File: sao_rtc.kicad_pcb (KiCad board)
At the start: 2 copper layers, 44.9 x 32.9 mm, 40 parts, among them J1 S2B-PH-K-S(LF)(SN), J2 Conn_02x03_Odd_Even, J3 Conn_02x03_Odd_Even, P1 USB_C_Plug_USB2.0, SW1 DPDT, U1 AW32001ECSR, U2 PCF8563DRG, U3 M3410, Y1 32.768 kHz

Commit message: Complete 1st Draft
First Draft at Schematic Capture and Layout
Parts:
- removed C3: 1μF, sao:C_0603_1608Metric
- removed C4, C8: 4.7μF, sao:C_0603_1608Metric
- removed C5: C, Capacitor_THT:C_Disc_D3.0mm_W1.6mm_P2.50mm
- removed CLK0, VMON1: TestPoint, TestPoint:TestPoint_Loop_D2.50mm_Drill1.0mm
- removed D2: 4.3V, Diode_SMD:D_SOD-323_HandSoldering
- removed R2, R5: Ω, Resistor_SMD:R_0603_1608Metric
- removed R4: 10kΩ, Resistor_SMD:R_0603_1608Metric
- removed SW1: DPDT, Button_Switch_SMD:SW_DPDT_CK_JS202011JCQN
- removed TH1: Thermistor_NTC, Resistor_SMD:R_0603_1608Metric
- added C12: 47nF, Capacitor_SMD:C_0603_1608Metric, F.Cu at (97.6, 71.4)
- added C13: 10uF, Capacitor_SMD:C_0603_1608Metric, F.Cu at (91.3, 74.0)
- added C14: 10uF, Capacitor_SMD:C_0603_1608Metric, F.Cu at (94.6, 76.9)
- added C15: 10uF, Capacitor_SMD:C_0603_1608Metric, F.Cu at (91.3, 75.6)
- added C16: 22uF, Capacitor_SMD:C_0603_1608Metric, F.Cu at (109.8, 79.0)
- added C17: 22uF, Capacitor_SMD:C_0603_1608Metric, F.Cu at (94.9, 80.7)
- added C18: 47nF, Capacitor_SMD:C_0603_1608Metric, F.Cu at (108.3, 88.4)
- added C19: 47nF, Capacitor_SMD:C_0603_1608Metric, F.Cu at (110.5, 88.4)
- added D6: D, Diode_SMD:D_SMA, F.Cu at (107.0, 60.0)
- added D7: STAT, LED_SMD:LED_0603_1608Metric, F.Cu at (82.4, 84.1)
- added FB1: FerriteBead, Inductor_SMD:L_TDK_NLV32_3.2x2.5mm, F.Cu at (109.0, 81.4)
- added JP1: PH2.54-1x3P, Connector_PinHeader_2.54mm:PinHeader_1x03_P2.54mm_Vertical, F.Cu at (82.5, 68.0)
- added L3: 1uH, Inductor_SMD:L_1008_2520Metric, F.Cu at (94.9, 74.6)
- added R10: 10kΩ, Resistor_SMD:R_0603_1608Metric, F.Cu at (85.5, 68.3)
- added R12: 5.36k, Resistor_SMD:R_0603_1608Metric, F.Cu at (86.0, 71.5)
- added R13: 31.6k, Resistor_SMD:R_0603_1608Metric, F.Cu at (86.0, 73.4)
- added R15: 22Ω, Resistor_SMD:R_0603_1608Metric, F.Cu at (82.4, 82.5)
- added R16: 10kΩ, Resistor_SMD:R_0603_1608Metric, F.Cu at (82.4, 89.1)
- added R17: 10kΩ, Resistor_SMD:R_0603_1608Metric, F.Cu at (82.4, 80.8)
- added R18: 232, Resistor_SMD:R_0603_1608Metric, F.Cu at (89.9, 71.6)
- added TP1: TestPoint, TestPoint:TestPoint_Loop_D2.60mm_Drill1.4mm_Beaded, F.Cu at (114.5, 80.0)
- added TP2: TestPoint, TestPoint:TestPoint_Loop_D2.60mm_Drill1.4mm_Beaded, F.Cu at (114.5, 75.0)
- added TP3: TP_BATT, TestPoint:TestPoint_Loop_D2.60mm_Drill1.4mm_Beaded, F.Cu at (82.5, 58.9)
- added TP4: TP_PGOOD, TestPoint:TestPoint_Loop_D2.60mm_Drill1.4mm_Beaded, F.Cu at (82.5, 63.5)
- added TP5: TP_BMS, TestPoint:TestPoint_Loop_D2.60mm_Drill1.4mm_Beaded, F.Cu at (82.7, 77.5)
- added TP6: TP_VMON, TestPoint:TestPoint_Loop_D2.60mm_Drill1.4mm_Beaded, F.Cu at (114.5, 70.0)
- added TP7: TP_3V3, TestPoint:TestPoint_Loop_D2.60mm_Drill1.4mm_Beaded, F.Cu at (114.5, 85.0)
- added U5: XB7608AJ, sao:CPC-5_2.6mmx4mm_P0.53mm, F.Cu at (87.1, 59.9)
- C1: value 2.2μF -> 22uF
- C11: value 12uF -> 1μF
- C2: footprint sao:C_0603_1608Metric -> Capacitor_SMD:C_0603_1608Metric
- C7: value ~ -> 10μF
- D5: value RTC ON -> PGOOD
- J2: value Conn_02x03_Odd_Even -> Connector, In
- J3: value Conn_02x03_Odd_Even -> Connector, Out; footprint Swadge_Parts:PinSocket_2x03_P2.54mm_Vertical -> sao:PinHeader_2x03_P2.54mm_Vertical_Flipped
- L2: footprint Inductor_SMD:L_0603_1608Metric -> Inductor_SMD:L_1008_2520Metric
- U1: value AW32001ECSR -> BQ24259; footprint Package_CSP:WLCSP-9_1.21x1.22mm_Layout3x3_P0.4mm -> Package_DFN_QFN:HVQFN-24-1EP_4x4mm_P0.5mm_EP2.6x2.6mm_ThermalVias
- U3: value M3410 -> MT3410
- moved R14 43.2 mm to (82.4, 87.4)
- moved D5 43.1 mm to (82.4, 85.8)
- moved R11 39.2 mm to (82.4, 90.8), turned to 0 degrees
- moved D4 38.3 mm to (82.4, 92.5), turned to 180 degrees
- moved C11 32.1 mm to (95.5, 66.0), turned to 0 degrees
- moved R7 24.6 mm to (112.1, 58.4), turned to 90 degrees
- moved R6 22.2 mm to (112.1, 61.7)
- moved R8 17.4 mm to (97.3, 82.1), turned to -90 degrees
- moved C7 13.9 mm to (97.8, 68.2), turned to 90 degrees
- moved C1 13.5 mm to (108.4, 73.9), turned to 90 degrees
- moved U2 12.1 mm to (104.7, 71.6), turned to -90 degrees
- moved C9 11.9 mm to (100.7, 77.6)
- moved R9 11.8 mm to (99.7, 83.0), turned to 0 degrees
- moved C2 10.9 mm to (99.2, 71.4), turned to -90 degrees
- moved D3 10.7 mm to (97.5, 62.0)
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- renumbered R12 to R14
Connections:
- net Net-(U2-OSCI) renamed /RTC/OSCI
- net Net-(U3-FB) renamed /3V3_REG/FB
- C1 pad 1: VDD -> /RTC/V_RTC
- C10 pad 1: Net-(C10-Pad1) -> /3V3_REG/3V3_SW
- C11 pad 1: 3V3 SAO -> +5V
- C2 pad 1: +5V -> /BMS/REGN
- C7 pad 1: Net-(U2-OSCO) -> /BMS/PMID
- C9 pad 1: SNODE -> /VBMS
- D1 pad 1: BATT+ -> /BATT+
- D4 pad 2: 3V3 SAO -> 3V3
- D5 pad 2: VDD -> 3V3
- F1 pad 1: SNODE -> /BMS/VSYS
- F1 pad 2: Net-(D2-K) -> /VBMS
- J1 pad 1: BATT+ -> /BATT+
- J1 pad 2: GND -> Net-(J1-Pad2)
- J2 pad 3: SDA -> /SDA
- J2 pad 4: SCL -> /SCL
- J3 pad 3: SDA -> /SDA
- J3 pad 4: SCL -> /SCL
- L1 pad 1: Net-(C10-Pad1) -> /3V3_REG/3V3_SW
- L2 pad 1: 3V3 SAO -> 3V3
- L2 pad 2: Net-(C10-Pad1) -> /3V3_SAO
- R14 pad 1: GND -> /~{PG}
- R7 pad 2: SNODE -> /BATT+
- R9 pad 2: Net-(C10-Pad1) -> /3V3_REG/3V3_SW
- U2 pad 2: Net-(U2-OSCO) -> /RTC/OSCO
- U2 pad 3: unconnected-(U2-~{INT}-Pad3) -> /RTC/~{INT}
- U2 pad 5: SDA -> /SDA
- U2 pad 6: SCL -> /SCL
- U2 pad 7: Net-(U2-CLKO) -> /RTC/CLK0
- U2 pad 8: VDD -> /RTC/V_RTC
- U3 pad 1: SNODE -> /VBMS
- U3 pad 4: SNODE -> /VBMS
- Y1 pad 1: Net-(U2-OSCO) -> /RTC/OSCO
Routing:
- net /SDA: track 0.00 -> 95.7 mm, vias 0 -> 2
- net /SCL: track 0.00 -> 92.6 mm, vias 0 -> 3
- net SCL: track 71.0 -> 0.00 mm, vias 4 -> 0
- net /BATT+: track 0.00 -> 69.2 mm, vias 0 -> 3
- net SDA: track 59.9 -> 0.00 mm, vias 3 -> 0
- net GND: track 9.49 -> 62.5 mm, vias 54 -> 63
- net /~{PG}: track 0.00 -> 40.1 mm, vias 0 -> 2
- net /RTC/~{INT}: track 0.00 -> 30.9 mm
- net /STAT: track 0.00 -> 30.6 mm, vias 0 -> 2
- net VDD: track 23.9 -> 0.00 mm, vias 3 -> 0
- net /BMS/VSYS: track 0.00 -> 21.0 mm
- net /RTC/V_RTC: track 0.00 -> 16.3 mm
- net 3V3: track 40.6 -> 56.5 mm, vias 0 -> 3
- net /RTC/CLK0: track 0.00 -> 13.6 mm
- net Net-(D2-A): track 13.3 -> 0.00 mm, vias 2 -> 0
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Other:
- board size 44.9 x 32.9 mm -> 37.5 x 43 mm
- board text added: "If using Lithium battery, please turn swadge OFF or remove AAs This board WILL power the swadge"
- board text added: "RTC and BMS SAO rev 1 7/4/2026"
- board text removed: "BMS"
- board text removed: "If using Lithium battery, please turn swadge OFF or remove AAs This board can power the swadge"
- board text removed: "RTC and BMS SAO rev 0 6/3/2026"
- board text removed: "Up -> Power from Battery Down -> Power from Swadge"

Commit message: Silkscreen Updates
Changed Silk
Made it slightly smaller
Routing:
- net /SCL: vias 3 -> 2
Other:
- board size 37.5 x 43 mm -> 37 x 43 mm
- board text added: "-STAT"
- board text added: "-~{PG}"
- board text added: "3V3"
- board text added: "BATT"
- board text added: "BMS_INT"
- board text added: "RTC_CLK"
- board text added: "VMON"
- board text added: "VSYS"
- board text added: "~{INT}"

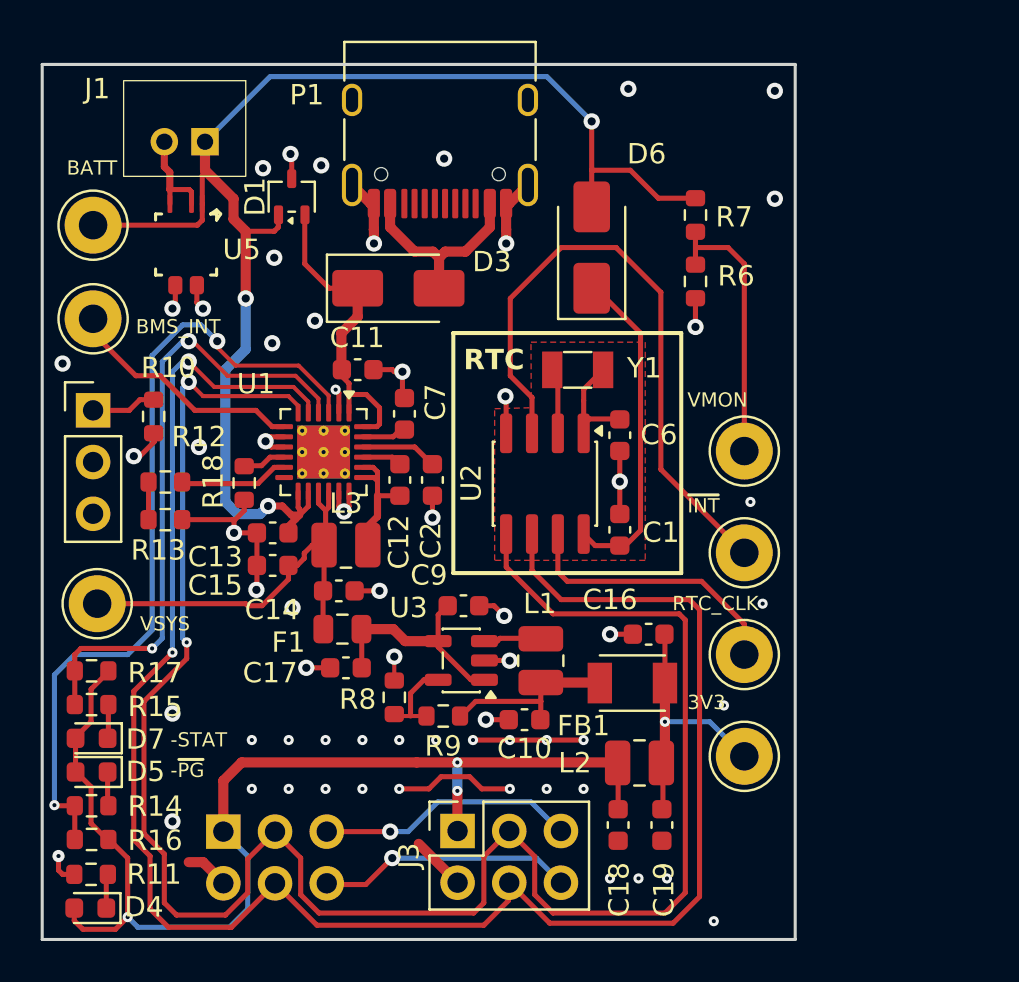
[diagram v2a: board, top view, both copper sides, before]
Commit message: DRC Fixes
Changes to Via Size to 0.25, need to evaluate to 0.3
Changes to Text Size
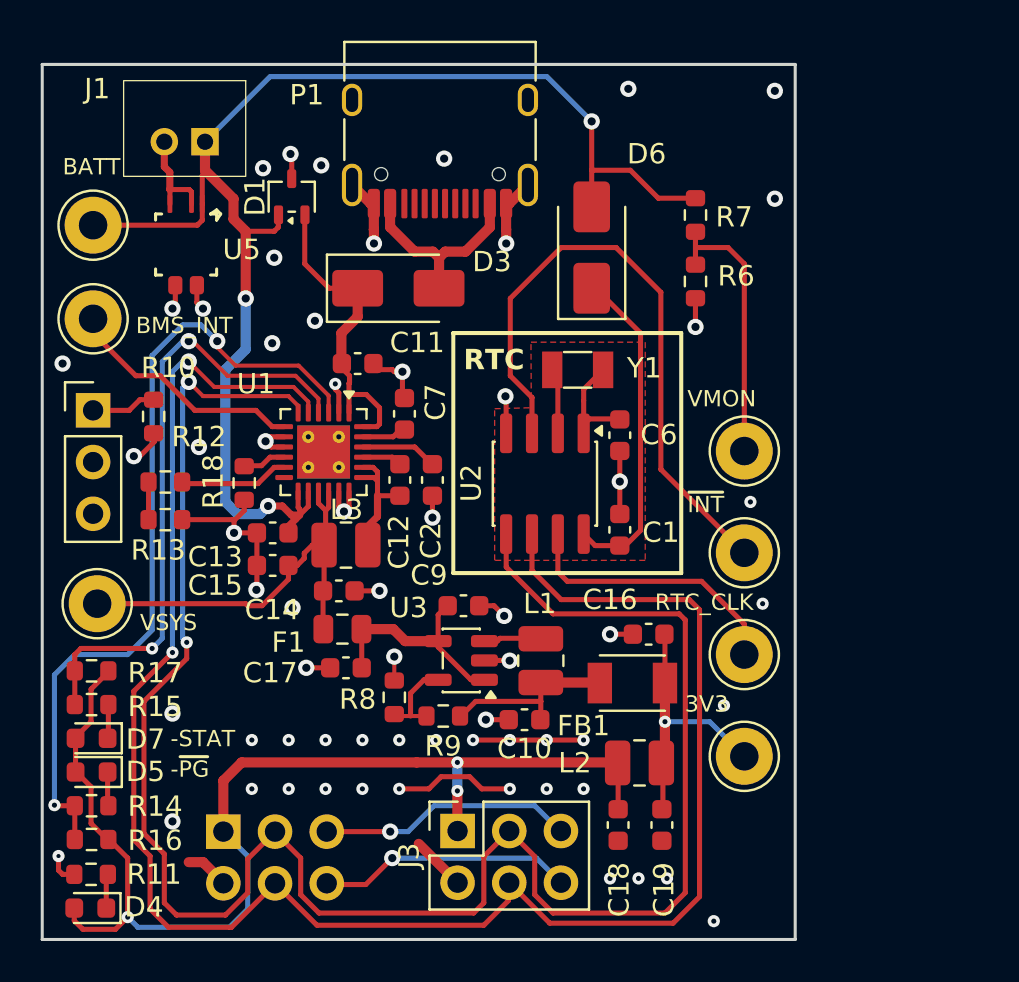
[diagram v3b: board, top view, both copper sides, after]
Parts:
- moved C11 0.30 mm to (95.5, 65.7)
